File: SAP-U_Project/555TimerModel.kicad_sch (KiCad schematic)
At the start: 9 parts, among them Q1 BC107, U1 Comparator, U2 SR LATCH

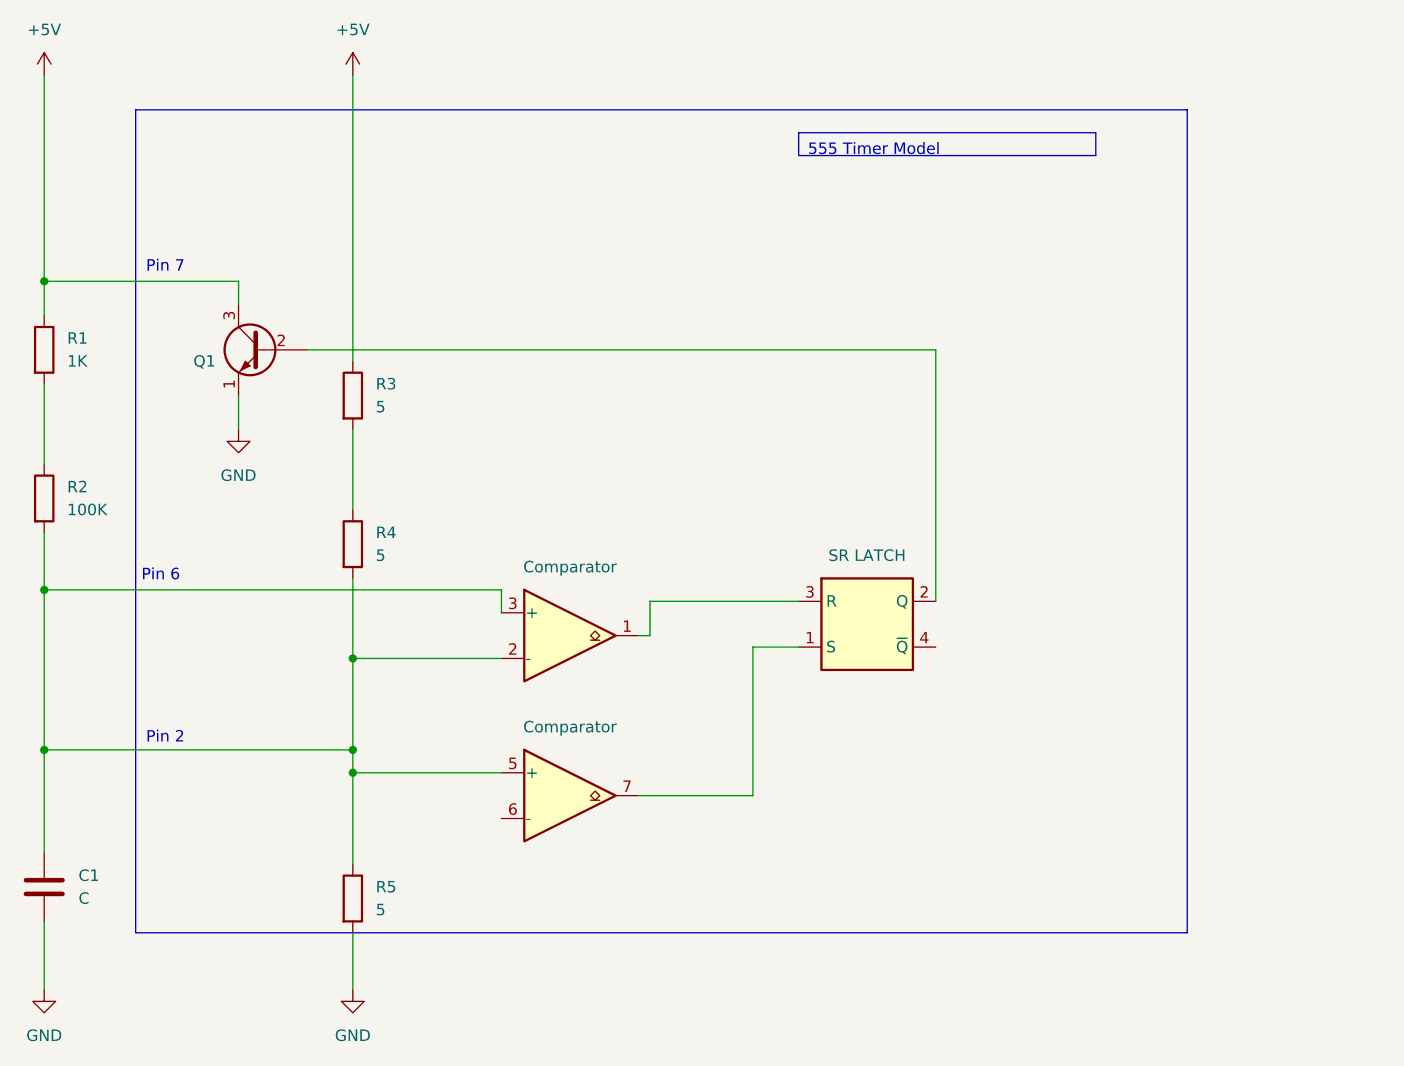
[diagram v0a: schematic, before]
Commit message: Checkpoint: created documentation and schematic for the astable portion of the clock module
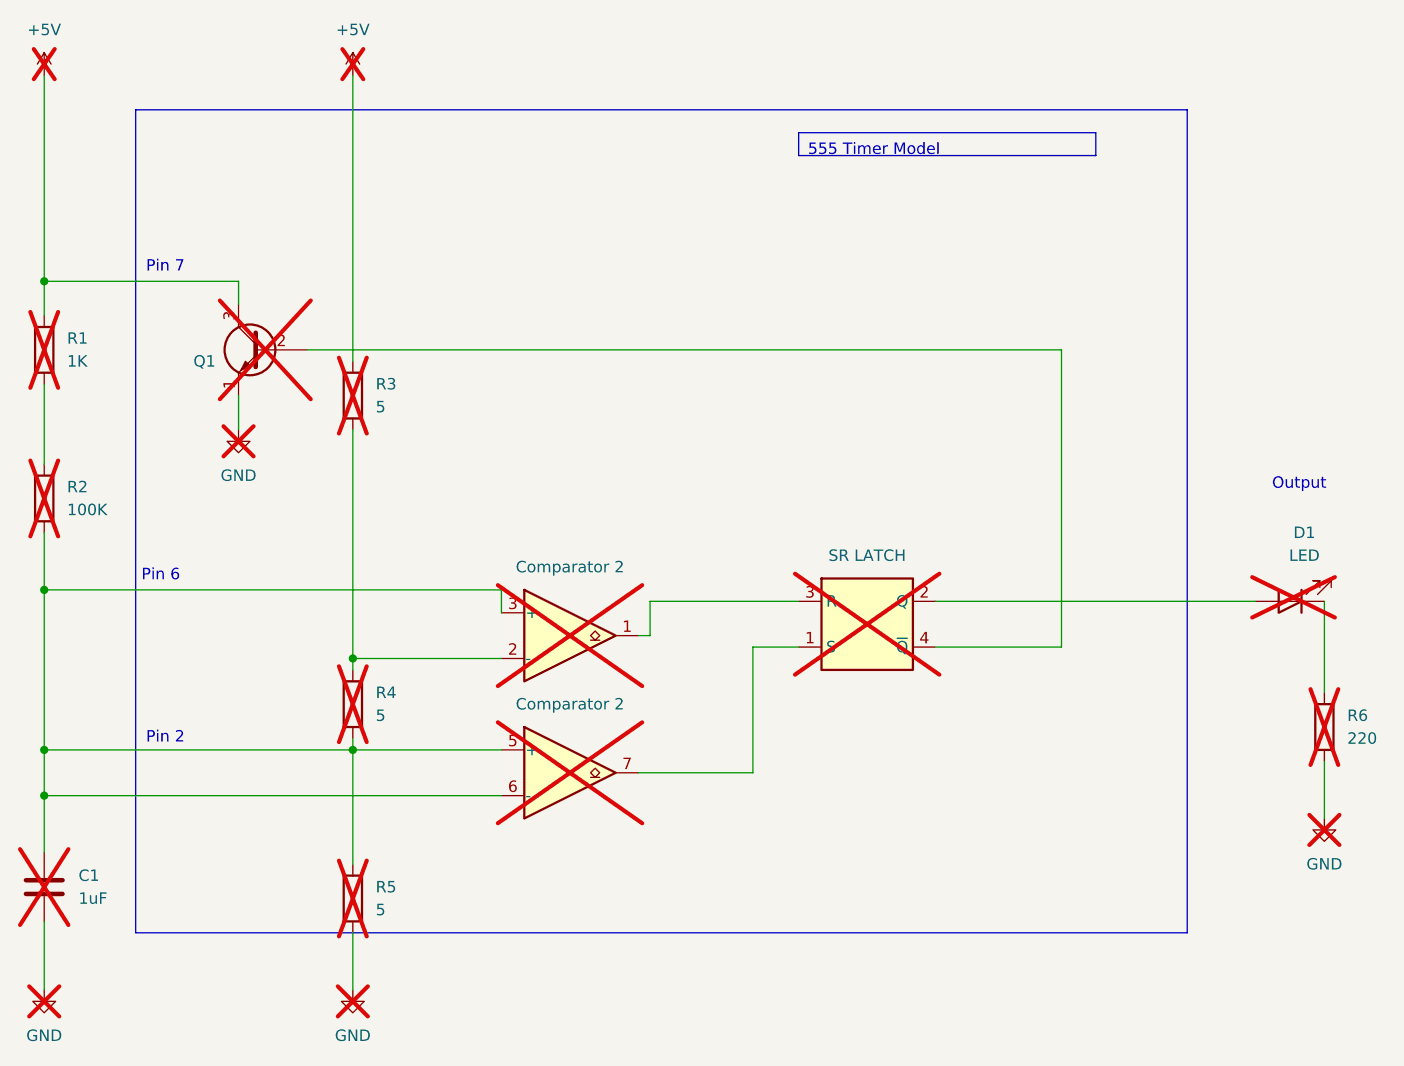
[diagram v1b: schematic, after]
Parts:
- added D1: LED, symbol Device:LED
- added R6: 220, symbol Device:R
- C1: value C -> 1uF; now not fitted; now left out of the parts list
- Q1, R1, R2, R3, R4, R5, U2: now not fitted; now left out of the parts list
- U1: value Comparator -> Comparator 2; now not fitted; now left out of the parts list
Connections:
- net GND: now also R6.2
- net at R3.2, R4.1: now also U1.2 (-)
- net at C1.1, R2.2, R4.2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: now also U1.6 (-); no longer U1.2 (-)
- net at Q1.2 (B): now also U2.4 (~{Q}); no longer U2.2 (Q)
- new net: D1.1 (K), R6.1
- new net: D1.2 (A), U2.2 (Q)
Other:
- note added: "Output"
